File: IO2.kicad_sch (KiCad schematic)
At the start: 35 parts, among them J901 Conn_01x03_Pin, J902 Conn_01x03_Pin, J903 Conn_01x03_Pin, J904 Conn_01x03_Pin, J905 Conn_01x03_Pin, J906 Conn_01x03_Pin, J907 Conn_01x03_Pin, J908 Conn_01x03_Pin, J909 Conn_01x03_Pin, J910 Conn_01x03_Pin, J911 Conn_01x03_Pin, J912 Conn_01x03_Pin, J913 12402012E212A, J914 SM04B-GHS-TB(LF)(SN), U901 USBLC6-2P6

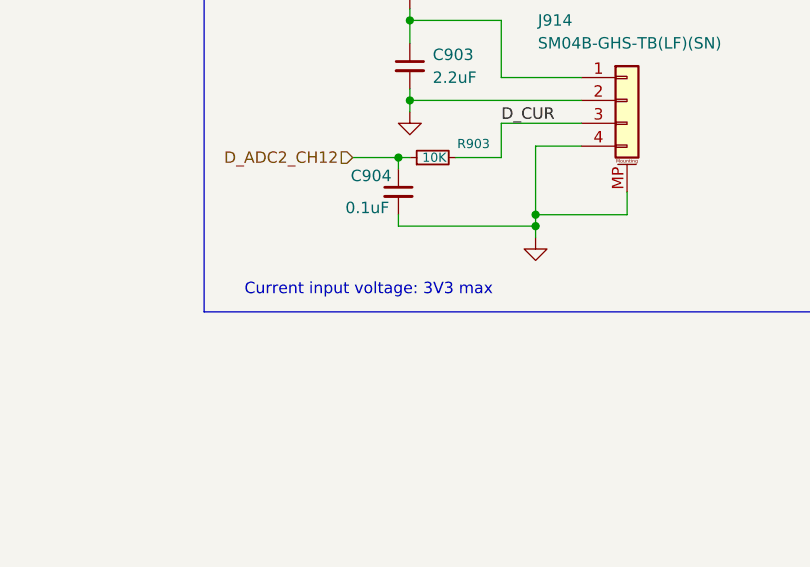
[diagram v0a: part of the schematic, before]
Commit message: feat: add layout notes and net labels
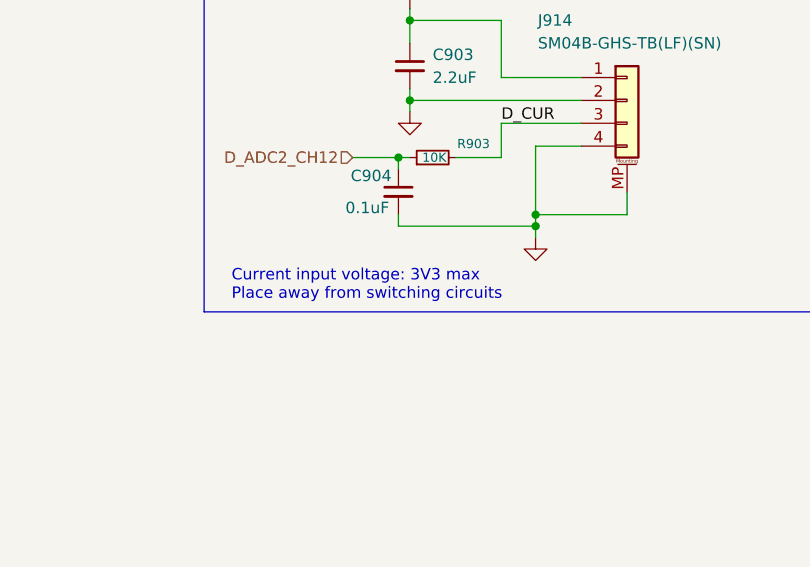
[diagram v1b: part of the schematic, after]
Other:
- note added: "Current input voltage: 3V3 max Place away from switching circuits"
- note removed: "Current input voltage: 3V3 max"
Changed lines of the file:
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@@
 		)
 	)
-	(text "Current input voltage: 3V3 max"
+	(text "Current input voltage: 3V3 max\nPlace away from switching circuits"
 		(exclude_from_sim no)
-		(at 187.198 151.892 0)
+		(at 171.958 151.384 0)
 		(effects
 			(font
 				(size 1.27 1.27)
 			)
+			(justify left)
 		)
 	)

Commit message: refactor: change name from FeroFly405 to FeroFlyF405
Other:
- title: FeroFly405 -> FeroFlyF405

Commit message: fix: CAN ESD diode connection
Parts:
- J901, J902, J903, J904, J905, J906, J907, J908, J909, J910, J911, J912: footprint Connector_PinHeader_2.54mm:PinHeader_1x03_P2.54mm_Vertical -> pin_header_01x03:PinHeader_1x03_P2.54mm_Vertical
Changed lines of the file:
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@@
 			)
 		)
-		(property "Footprint" "Connector_PinHeader_2.54mm:PinHeader_1x03_P2.54mm_Vertical"
+		(property "Footprint" "pin_header_01x03:PinHeader_1x03_P2.54mm_Vertical"
 			(at 64.77 53.34 0)
 			(hide yes)
@@
 			)
 		)
-		(property "Footprint" "Connector_PinHeader_2.54mm:PinHeader_1x03_P2.54mm_Vertical"
+		(property "Footprint" "pin_header_01x03:PinHeader_1x03_P2.54mm_Vertical"
 			(at 64.77 91.44 0)
 			(hide yes)
@@
 			)
 		)
-		(property "Footprint" "Connector_PinHeader_2.54mm:PinHeader_1x03_P2.54mm_Vertical"
+		(property "Footprint" "pin_header_01x03:PinHeader_1x03_P2.54mm_Vertical"
 			(at 64.77 66.04 0)
 			(hide yes)
@@
 			)
 		)
-		(property "Footprint" "Connector_PinHeader_2.54mm:PinHeader_1x03_P2.54mm_Vertical"
+		(property "Footprint" "pin_header_01x03:PinHeader_1x03_P2.54mm_Vertical"
 			(at 64.77 40.64 0)
 			(hide yes)
@@
 			)
 		)
-		(property "Footprint" "Connector_PinHeader_2.54mm:PinHeader_1x03_P2.54mm_Vertical"
+		(property "Footprint" "pin_header_01x03:PinHeader_1x03_P2.54mm_Vertical"
 			(at 64.77 116.84 0)
 			(hide yes)
@@
 			)
 		)
-		(property "Footprint" "Connector_PinHeader_2.54mm:PinHeader_1x03_P2.54mm_Vertical"
+		(property "Footprint" "pin_header_01x03:PinHeader_1x03_P2.54mm_Vertical"
 			(at 64.77 154.94 0)
 			(hide yes)
@@
 			)
 		)
-		(property "Footprint" "Connector_PinHeader_2.54mm:PinHeader_1x03_P2.54mm_Vertical"
+		(property "Footprint" "pin_header_01x03:PinHeader_1x03_P2.54mm_Vertical"
 			(at 64.77 142.24 0)
 			(hide yes)
@@
 			)
 		)
-		(property "Footprint" "Connector_PinHeader_2.54mm:PinHeader_1x03_P2.54mm_Vertical"
+		(property "Footprint" "pin_header_01x03:PinHeader_1x03_P2.54mm_Vertical"
 			(at 64.77 180.34 0)
 			(hide yes)
@@
 			)
 		)
-		(property "Footprint" "Connector_PinHeader_2.54mm:PinHeader_1x03_P2.54mm_Vertical"
+		(property "Footprint" "pin_header_01x03:PinHeader_1x03_P2.54mm_Vertical"
 			(at 64.77 129.54 0)
 			(hide yes)
@@
 			)
 		)
-		(property "Footprint" "Connector_PinHeader_2.54mm:PinHeader_1x03_P2.54mm_Vertical"
+		(property "Footprint" "pin_header_01x03:PinHeader_1x03_P2.54mm_Vertical"
 			(at 64.77 167.64 0)
 			(hide yes)
@@
 			)
 		)
-		(property "Footprint" "Connector_PinHeader_2.54mm:PinHeader_1x03_P2.54mm_Vertical"
+		(property "Footprint" "pin_header_01x03:PinHeader_1x03_P2.54mm_Vertical"
 			(at 64.77 104.14 0)
 			(hide yes)
@@
 			)
 		)
-		(property "Footprint" "Connector_PinHeader_2.54mm:PinHeader_1x03_P2.54mm_Vertical"
+		(property "Footprint" "pin_header_01x03:PinHeader_1x03_P2.54mm_Vertical"
 			(at 64.77 78.74 0)
 			(hide yes)

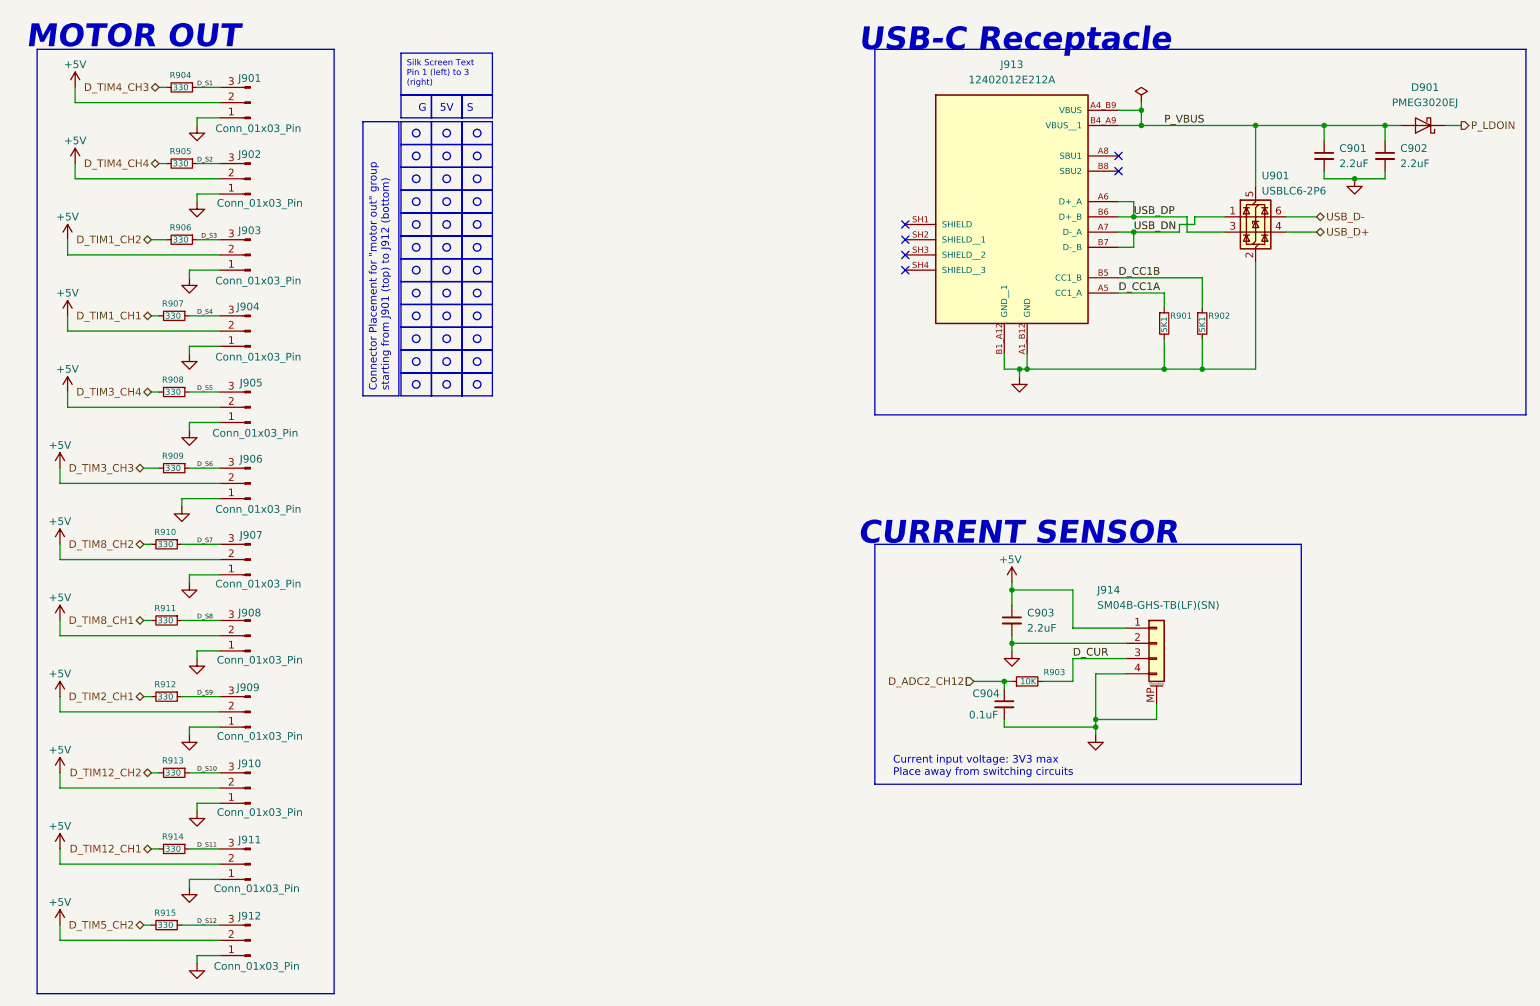
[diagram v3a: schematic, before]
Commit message: refactor: change motor output, renamed power nets
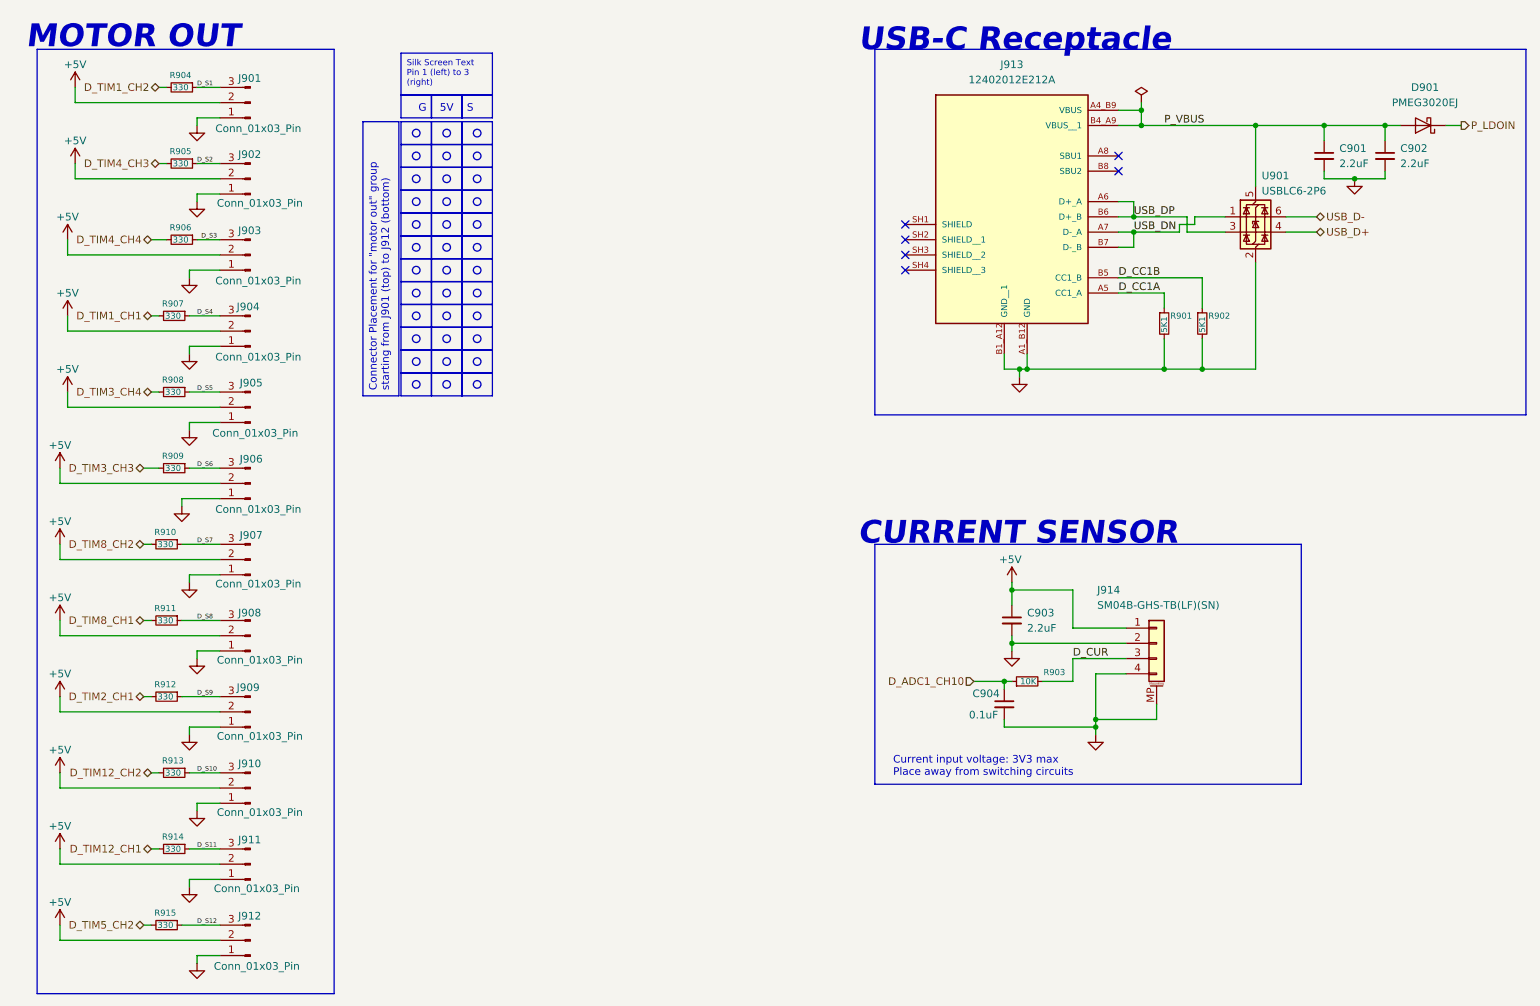
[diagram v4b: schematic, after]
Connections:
- net D_TIM1_CH2: now also R904.2; no longer R906.2
- net D_TIM4_CH3: now also R905.2; no longer R904.2
- net D_TIM4_CH4: now also R906.2; no longer R905.2
- net D_ADC2_CH12 renamed D_ADC1_CH10
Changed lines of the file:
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@@
 	(hierarchical_label "D_TIM1_CH2"
 		(shape bidirectional)
-		(at 48.26 63.5 180)
+		(at 49.53 38.1 180)
 		(effects
 			(font
@@
 	(hierarchical_label "D_TIM4_CH3"
 		(shape bidirectional)
-		(at 49.53 38.1 180)
+		(at 49.53 50.8 180)
 		(effects
 			(font
@@
 		)
 	)
-	(hierarchical_label "D_ADC2_CH12"
+	(hierarchical_label "D_ADC1_CH10"
 		(shape input)
 		(at 185.42 137.16 180)
@@
 	(hierarchical_label "D_TIM4_CH4"
 		(shape bidirectional)
-		(at 49.53 50.8 180)
+		(at 48.26 63.5 180)
 		(effects
 			(font
